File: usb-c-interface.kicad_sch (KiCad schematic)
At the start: 77 parts, among them IC1 TPS7A0518PDBVT, J3 12401598E4_2A, J4 12401598E4_2A, J5 12401598E4_2A, U5 FT232RQ-REEL, U7 NX3DV42GU

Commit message: Introduce component standardization
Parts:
- C58, C59, C62, C76, C78, C89, C96: renamed from C?; value (none) -> C_47u_0603; footprint (none) -> sa800u-baseboard-hw-footprints:C_0603_1608Metric; Author (none) -> Antmicro; License (none) -> Apache-2.0; Manufacturer MURATA -> Murata
- C60, C61, C63, C64, C65, C67, C69, C79, C80, C83, C84, C87, C88, C92, C93: footprint sa800u-baseboard-hw-footprints:0402-cap -> sa800u-baseboard-hw-footprints:C_0402_1005Metric; Author (none) -> Antmicro; Dielectric (none) -> X5R; License (none) -> Apache-2.0; MPN 0402X104K6R3CT -> GRM155R61H104KE14D; Manufacturer Walsin -> Murata; Voltage (none) -> 50V
- C66: footprint sa800u-baseboard-hw-footprints:0402-cap -> sa800u-baseboard-hw-footprints:C_0402_1005Metric; Author (none) -> Antmicro; License (none) -> Apache-2.0
- C68, C70: footprint sa800u-baseboard-hw-footprints:0402-cap -> sa800u-baseboard-hw-footprints:C_0402_1005Metric; Author (none) -> Antmicro; Dielectric (none) -> C0G; License (none) -> Apache-2.0; MPN C0402C470J5GACTU -> GRM1555C1E470JA01D; Manufacturer KEMET -> Murata
- C71: renamed from C?; value (none) -> C_10u_0402; footprint (none) -> sa800u-baseboard-hw-footprints:C_0402_1005Metric; Author (none) -> Antmicro; License (none) -> Apache-2.0; MPN GRM155R60J106ME44D -> CC0402MRX5R5BB106; Manufacturer MURATA -> Yaego
- C72, C73, C74: renamed from C?; value (none) -> C_100n_0402; footprint (none) -> sa800u-baseboard-hw-footprints:C_0402_1005Metric; Author (none) -> Antmicro; Dielectric (none) -> X5R; License (none) -> Apache-2.0; MPN 0402X104K6R3CT -> GRM155R61H104KE14D; Manufacturer Walsin -> Murata; Voltage (none) -> 50V
- C75: footprint sa800u-baseboard-hw-footprints:0603-cap -> sa800u-baseboard-hw-footprints:C_0603_1608Metric; Author (none) -> Antmicro; License (none) -> Apache-2.0; Manufacturer WALSIN -> Walsin
- C77: footprint sa800u-baseboard-hw-footprints:0603-cap -> sa800u-baseboard-hw-footprints:C_0603_1608Metric; Author (none) -> Antmicro; License (none) -> Apache-2.0
- C81, C82, C85, C86, C90, C91, C94, C95: value (none) -> C_100n_0402; footprint (none) -> sa800u-baseboard-hw-footprints:C_0402_1005Metric; Author (none) -> Antmicro; Dielectric (none) -> X5R; License (none) -> Apache-2.0; MPN 0402X104K6R3CT -> GRM155R61H104KE14D; Manufacturer Walsin -> Murata; Voltage (none) -> 50V
- D10, D11, D12, D7, D8, D9: renamed from D?; value (none) -> PUSB3F96X_PASS; footprint (none) -> sa800u-baseboard-hw-footprints:Nexperia_DFN-10_2.5x1mm_P0.5mm; Author (none) -> Antmicro; License (none) -> Apache-2.0
- D6: footprint sa800u-baseboard-hw-footprints:SOD-323F -> sa800u-baseboard-hw-footprints:D_SOD-323F; Author (none) -> Antmicro; License (none) -> Apache-2.0
- FB3: value BLM18EG221SN1D -> FB_220Z_1A_0603; footprint sa800u-baseboard-hw-footprints:0603 -> sa800u-baseboard-hw-footprints:FB_0603_1608Metric; symbol sa800u-baseboard-hw:BLM18EG221SN1D -> sa800u-baseboard-hw:FB_220Z_1A_0603; Author (none) -> Antmicro; License (none) -> Apache-2.0
- IC1: value TPS7A0518PDBVT -> TPS7A0518P_SOT23-5; symbol sa800u-baseboard-hw:TPS7A0518PDBVT -> sa800u-baseboard-hw:TPS7A0518P_SOT23-5; Author (none) -> Antmicro; License (none) -> Apache-2.0
- J3, J4, J5: footprint sa800u-baseboard-hw-footprints:USB-C_Female_12401X -> sa800u-baseboard-hw-footprints:USB-C_12401610E4_2A; Author (none) -> Antmicro; License (none) -> Apache-2.0; Manufacturer Amphenol ICC (Commercial Products) -> Amphenol
- R57, R58: footprint sa800u-baseboard-hw-footprints:0402-res -> sa800u-baseboard-hw-footprints:R_0402_1005Metric; Author (none) -> Antmicro; License (none) -> Apache-2.0; MPN CRCW0402100KFKEDHP -> CR0402-FX-1003GLF; Manufacturer VISHAY -> Bourns; Tolerance (none) -> 1%
- R59: renamed from R?; value (none) -> R_100k_0.5%_0402; footprint (none) -> sa800u-baseboard-hw-footprints:R_0402_1005Metric; Author (none) -> Antmicro; License (none) -> Apache-2.0; Manufacturer PANASONIC -> Panasonic
- R60, R61, R63: renamed from R?; value (none) -> R_100k_0402; footprint (none) -> sa800u-baseboard-hw-footprints:R_0402_1005Metric; Author (none) -> Antmicro; License (none) -> Apache-2.0; MPN CRCW0402100KFKEDHP -> CR0402-FX-1003GLF; Manufacturer VISHAY -> Bourns; Tolerance (none) -> 1%
- R62: footprint sa800u-baseboard-hw-footprints:0402-res -> sa800u-baseboard-hw-footprints:R_0402_1005Metric; Author (none) -> Antmicro; License (none) -> Apache-2.0; MPN RC0402FR-072K2L -> CR0402-FX-2201GLF; Manufacturer YAGEO -> Bourns; Tolerance (none) -> 1%
- R64: renamed from R?; value (none) -> R_200k_0402; footprint (none) -> sa800u-baseboard-hw-footprints:R_0402_1005Metric; Author (none) -> Antmicro; License (none) -> Apache-2.0; MPN RC0402FR-07200KL -> CR0402-FX-2003GLF; Manufacturer YAGEO_(PHYCOMP) -> Bourns; Tolerance (none) -> 1%
- TP100, TP101, TP102, TP103, TP104, TP105, TP106, TP107, TP108, TP109, TP110, TP111, TP99: renamed from TP?; value (none) -> TP_0.75mm_SMD; footprint (none) -> sa800u-baseboard-hw-footprints:TP_SMD_0.75mm; symbol sa800u-baseboard-hw:TP_SMD_0_75MM -> sa800u-baseboard-hw:TP_0.75mm_SMD; Author (none) -> Antmicro; License (none) -> Apache-2.0
- U5: value FT232RQ-REEL -> FT232R_QFN; symbol sa800u-baseboard-hw:FT232RQ-REEL -> sa800u-baseboard-hw:FT232R_QFN; Author (none) -> Antmicro; License (none) -> Apache-2.0; Manufacturer FTDI, Future Technology Devices International Ltd -> FTDI
- U6: renamed from U?; value (none) -> TPS25820DSST; footprint (none) -> sa800u-baseboard-hw-footprints:WSON-12-1EP_2x3mm_P0.5mm; Author (none) -> Antmicro; License (none) -> Apache-2.0
- U7: footprint sa800u-baseboard-hw-footprints:XQFN10-1.5x1.9mm -> sa800u-baseboard-hw-footprints:XQFN-10-1.4x1.8mm_P0.4mm; Author (none) -> Antmicro; License (none) -> Apache-2.0; Manufacturer (none) -> NXP
- U8: renamed from U?; value (none) -> TXB0104_UQFN; footprint (none) -> sa800u-baseboard-hw-footprints:UQFN-12_2x1.7mm_P0.4mm_Texas_RUT; symbol sa800u-baseboard-hw:TXB0104RUT -> sa800u-baseboard-hw:TXB0104_UQFN; Author (none) -> Antmicro; License (none) -> Apache-2.0
- U9: renamed from U?; value (none) -> CBTL02043ABQ,115; footprint (none) -> sa800u-baseboard-hw-footprints:DHVQFN-20-1EP_2.5x4.5_P0.5mm; Author (none) -> Antmicro; License (none) -> Apache-2.0
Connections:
- net DBG_USB_D_N: now also C68.1; no longer C68.2
- net DBG_USB_D_P: now also C70.1; no longer C70.2
- net GND: now also C68.2, C70.2; no longer C68.1, C70.1
- net USB1C_RX0_C_N: now also C87.1; no longer C87.2
- net USB1C_RX0_C_P: now also C92.1; no longer C92.2
- net USB1C_RX1_C_N: now also C84.2; no longer C84.1
- net USB1C_RX1_C_P: now also C80.2; no longer C80.1
- net USB1C_TX0_C_N: now also C79.2; no longer C79.1
- net USB1C_TX0_C_P: now also C83.2; no longer C83.1
- net USB1C_TX1_C_N: now also C93.1; no longer C93.2
- net USB1C_TX1_C_P: now also C88.1; no longer C88.2
- net USB1_SS_RX0_N: now also C87.2; no longer C87.1
- net USB1_SS_RX0_P: now also C92.2; no longer C92.1
- net USB1_SS_RX1_N: now also C84.1; no longer C84.2
- net USB1_SS_RX1_P: now also C80.1; no longer C80.2
- net USB1_SS_TX0_N: now also C79.1; no longer C79.2
- net USB1_SS_TX0_P: now also C83.1; no longer C83.2
- net USB1_SS_TX1_N: now also C93.2; no longer C93.1
- net USB1_SS_TX1_P: now also C88.2; no longer C88.1
- net USB2C_RX1_C_N: now also C90.2; no longer C90.1
- net USB2C_RX1_C_P: now also C94.2; no longer C94.1
- net USB2C_RX1_N: now also C90.1; no longer C90.2
- net USB2C_RX1_P: now also C94.1; no longer C94.2
- net USB2C_RX2_C_N: now also C86.2; no longer C86.1
- net USB2C_RX2_C_P: now also C82.2; no longer C82.1
- net USB2C_RX2_N: now also C86.1; no longer C86.2
- net USB2C_RX2_P: now also C82.1; no longer C82.2
- net USB2C_TX1_C_N: now also C81.2; no longer C81.1
- net USB2C_TX1_C_P: now also C85.2; no longer C85.1
- net USB2C_TX1_N: now also C81.1; no longer C81.2
- net USB2C_TX1_P: now also C85.1; no longer C85.2
- net USB2C_TX2_C_N: now also C95.2; no longer C95.1
- net USB2C_TX2_C_P: now also C91.2; no longer C91.1
- net USB2C_TX2_N: now also C95.1; no longer C95.2
- net USB2C_TX2_P: now also C91.1; no longer C91.2
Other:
- moved on the sheet: C58, C59, C60, C61, C62, C63, C64, C65, C66, C67, C68, C69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

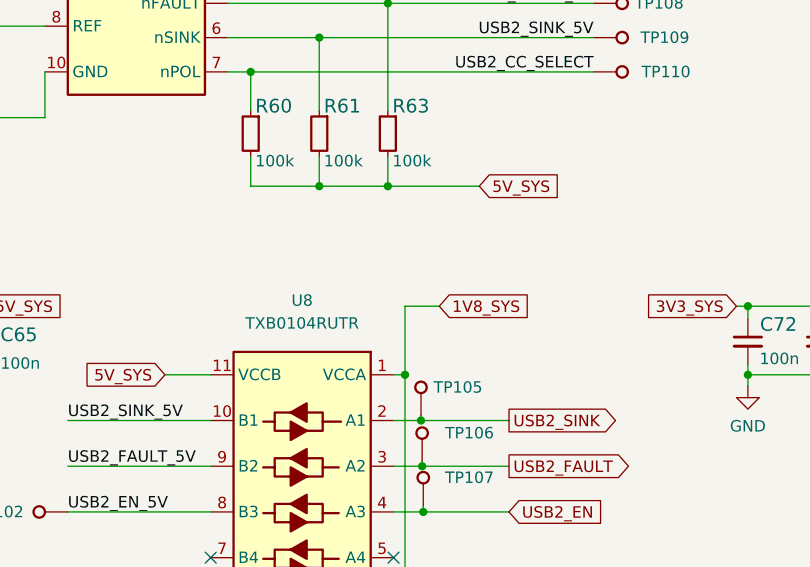
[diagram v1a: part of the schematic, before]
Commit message: Add OHP assets
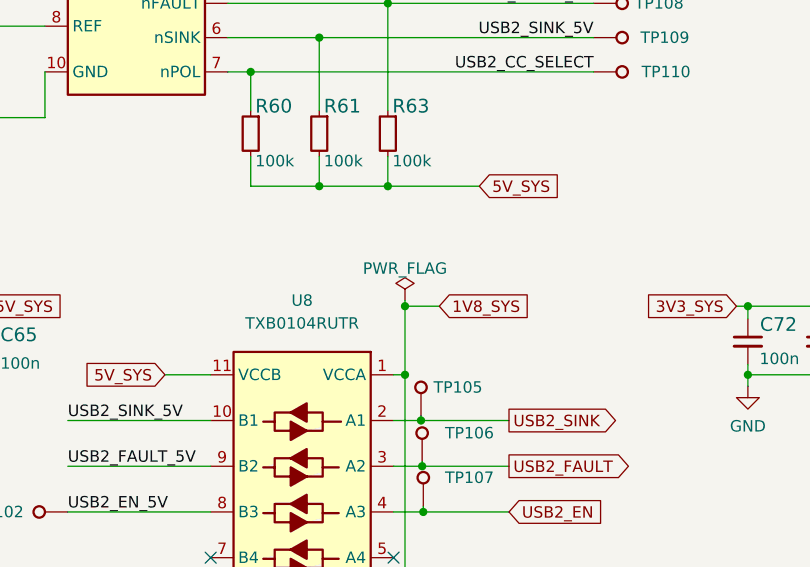
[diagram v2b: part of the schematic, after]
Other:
- company: (none) -> Antmicro Ltd.
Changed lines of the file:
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@@
   (title_block
     (title "SA800U (Snapdragon 845) Baseboard")
-    (date "2023-07-27")
-    (rev "1.0.2")
+    (date "2023-10-19")
+    (rev "1.0.3")
+    (company "Antmicro Ltd.")
     (comment 1 "www.antmicro.com")
-    (comment 2 "Antmicro Ltd.")
   )
   (junction (at 107.95 63.5) (diameter 0) (color 0 0 0 0)
@@
   (junction (at 109.982 123.825) (diameter 0) (color 0 0 0 0)
   )
+  (junction (at 113.665 236.855) (diameter 0) (color 0 0 0 0)
+  )
   (junction (at 316.865 233.045) (diameter 0) (color 0 0 0 0)
   )
@@
     (stroke (width 0) (type default) (color 0 0 0 0))
   )
+  (wire (pts (xy 113.665 236.22) (xy 113.665 236.855))
+    (stroke (width 0) (type default) (color 0 0 0 0))
+  )
   (wire (pts (xy 375.539 64.77) (xy 387.35 64.77))
     (stroke (width 0) (type default) (color 0 0 0 0))
@@
     (pin "2")
   )
-  (symbol (lib_id "sa800u-baseboard-hw:12401598E4_2A") (at 344.043 130.81 0) (mirror y) (unit 1)
+  (symbol (lib_name "12401598E4_2A_2") (lib_id "sa800u-baseboard-hw:12401598E4_2A") (at 344.043 130.81 0) (mirror y) (unit 1)
     (in_bom yes) (on_board yes) (fields_autoplaced)
     (property "Reference" "J5" (id 0) (at 332.6765 118.11 0))
@@
     (pin "SH")
   )
-  (symbol (lib_id "sa800u-baseboard-hw:12401598E4_2A") (at 342.773 59.69 0) (mirror y) (unit 1)
+  (symbol (lib_name "12401598E4_2A_1") (lib_id "sa800u-baseboard-hw:12401598E4_2A") (at 342.773 59.69 0) (mirror y) (unit 1)
     (in_bom yes) (on_board yes) (fields_autoplaced)
     (property "Reference" "J3" (id 0) (at 331.4065 46.99 0))
@@
     )
     (pin "1")
+  )
+  (symbol (lib_id "sa800u-baseboard-hw:PWR_FLAG") (at 113.665 236.22 0) (unit 1)
+    (in_bom yes) (on_board yes)
+    (property "Reference" "#FLG0108" (id 0) (at 113.665 234.315 0)
+      (effects (font (size 1.27 1.27)) hide)
+    )
+    (property "Value" "PWR_FLAG" (id 1) (at 113.665 232.664 0))
+    (property "Footprint" "" (id 2) (at 113.665 236.22 0)
+      (effects (font (size 1.27 1.27)) hide)
+    )
+    (property "Datasheet" "~" (id 3) (at 113.665 236.22 0)
+      (effects (font (size 1.27 1.27)) hide)
+    )
+    (pin "1")
